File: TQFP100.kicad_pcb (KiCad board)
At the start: 2 copper layers, 0 parts

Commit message: Connected all traces
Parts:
- added IC1: 100-PQFP, Package_QFP:PQFP-100_14x20mm_P0.65mm, F.Cu at (152.0, 81.8)
- added J1: Conn_02x15_Counter_Clockwise, Connector_PinHeader_2.54mm:PinHeader_2x15_P2.54mm_Vertical, F.Cu at (134.5, 98.0)
- added J2: Conn_02x10_Odd_Even_MountingPin, Connector_PinHeader_2.54mm:PinHeader_2x10_P2.54mm_Vertical, F.Cu at (175.2, 92.9)
- added J3: Conn_02x15_Counter_Clockwise, Connector_PinHeader_2.54mm:PinHeader_2x15_P2.54mm_Vertical, F.Cu at (170.1, 65.0)
- added J4: Conn_02x10_Odd_Even_MountingPin, Connector_PinHeader_2.54mm:PinHeader_2x10_P2.54mm_Vertical, F.Cu at (129.4, 70.0)
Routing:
- net Net-(IC1-VSS_5): track 0.00 -> 16.2 mm
- net Net-(IC1-A05): track 0.00 -> 15.3 mm
- net Net-(IC1-~{INTAK}): track 0.00 -> 15.1 mm
- net Net-(IC1-D15): track 0.00 -> 14.9 mm
- net Net-(IC1-A22): track 0.00 -> 14.7 mm
- net Net-(IC1-~{LMCS}): track 0.00 -> 14.6 mm
- net Net-(IC1-~{BREQ}): track 0.00 -> 14.5 mm
- net Net-(IC1-A20): track 0.00 -> 14.2 mm
- net Net-(J1-Pin_29): track 0.00 -> 14.1 mm
- net Net-(IC1-A03): track 0.00 -> 14.1 mm
- net Net-(IC1-~{MCS1}): track 0.00 -> 14.1 mm
- net Net-(IC1-~{INT3}): track 0.00 -> 14.0 mm
- net Net-(IC1-A07): track 0.00 -> 13.8 mm
- net Net-(IC1-A24): track 0.00 -> 13.7 mm
- net Net-(IC1-D13): track 0.00 -> 13.7 mm
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
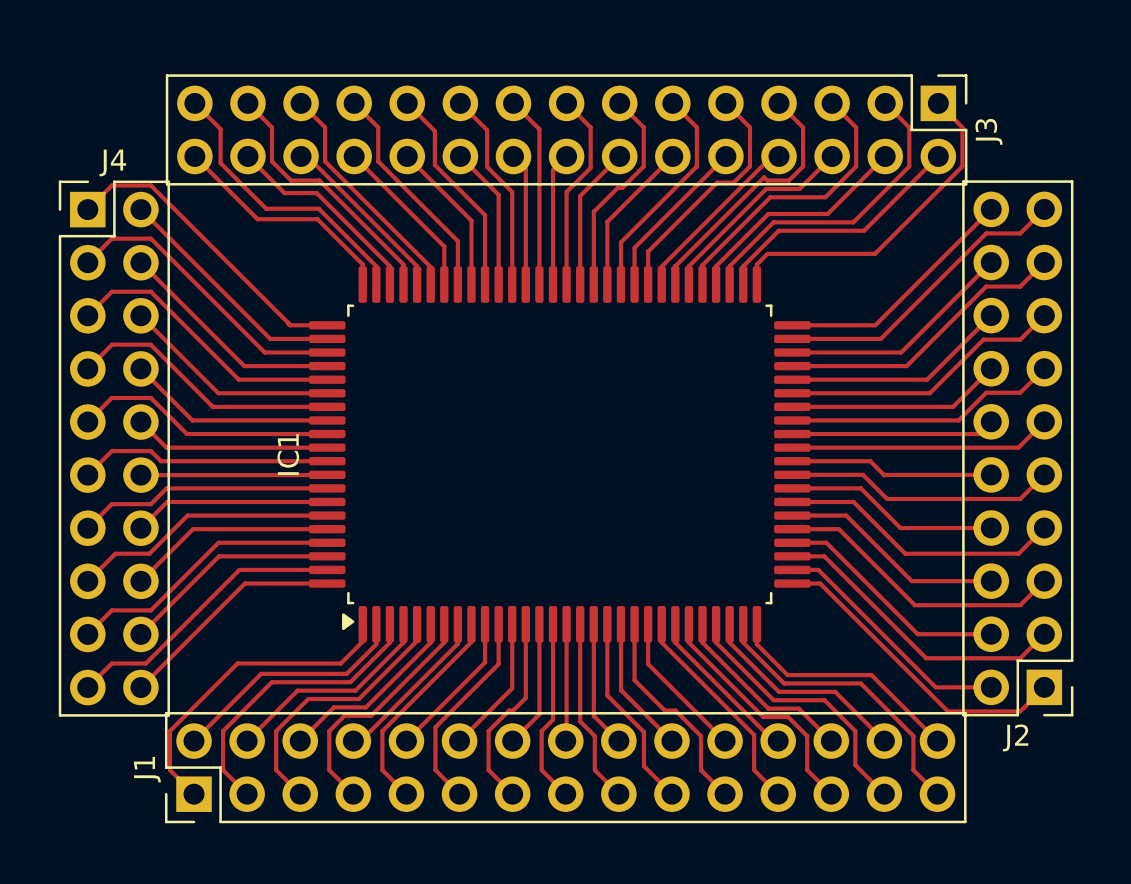
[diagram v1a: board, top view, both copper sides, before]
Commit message: Fixed the whole board, with correct names
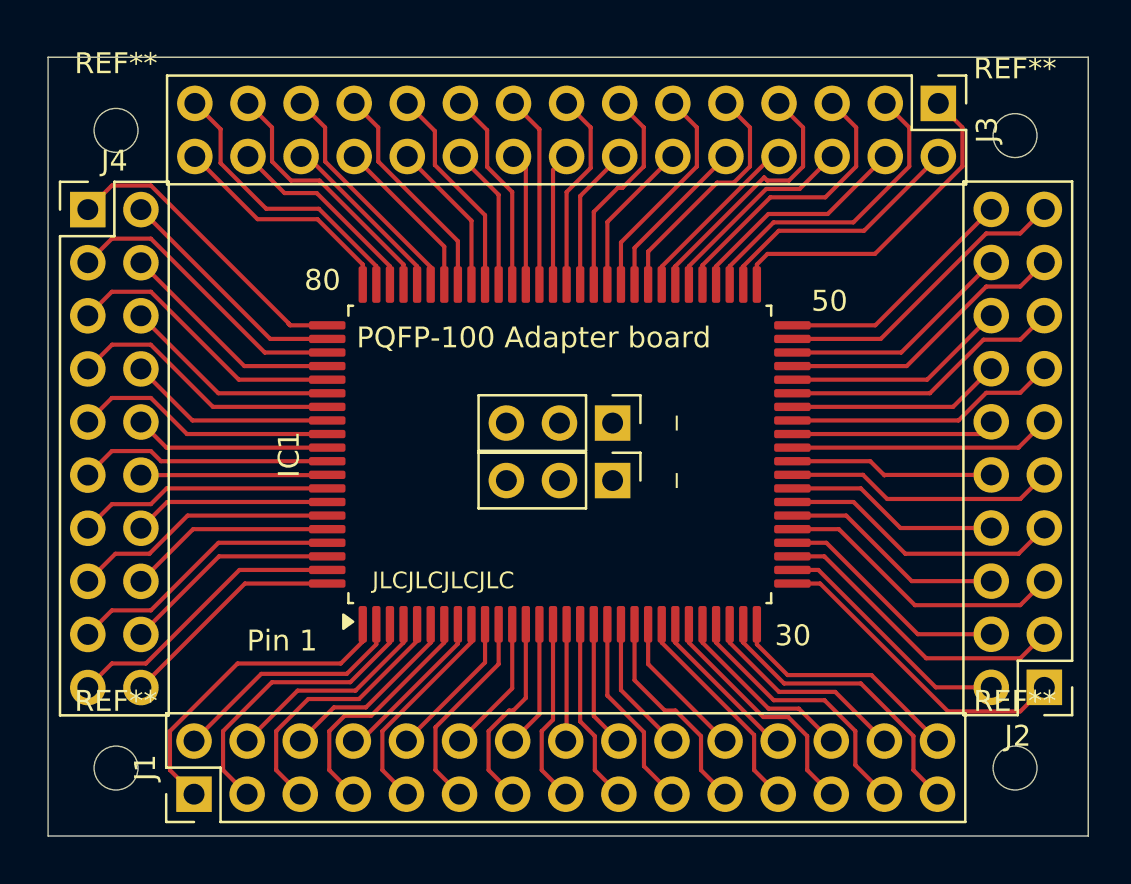
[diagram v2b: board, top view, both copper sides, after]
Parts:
- added REF**: MountingHole_2.1mm, MountingHole:MountingHole_2.1mm, F.Cu at (173.8, 96.8)
- added REF**: MountingHole_2.1mm, MountingHole:MountingHole_2.1mm, F.Cu at (130.8, 66.2)
- added REF**: MountingHole_2.1mm, MountingHole:MountingHole_2.1mm, F.Cu at (130.8, 96.8)
- added REF**: MountingHole_2.1mm, MountingHole:MountingHole_2.1mm, F.Cu at (173.8, 66.5)
- added _: PinHeader_1x03_P2.54mm_Vertical, Connector_PinHeader_2.54mm:PinHeader_1x03_P2.54mm_Vertical, F.Cu at (154.5, 83.0)
- added _: PinHeader_1x03_P2.54mm_Vertical, Connector_PinHeader_2.54mm:PinHeader_1x03_P2.54mm_Vertical, F.Cu at (154.5, 80.2)
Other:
- board outline added: 49.8 x 37.2 mm
- board text added: "30"
- board text added: "50"
- board text added: "80"
- board text added: "JLCJLCJLCJLC"
- board text added: "PQFP-100 Adapter board"
- board text added: "Pin 1"

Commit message: Larger pads to accommodate more ic, rev3
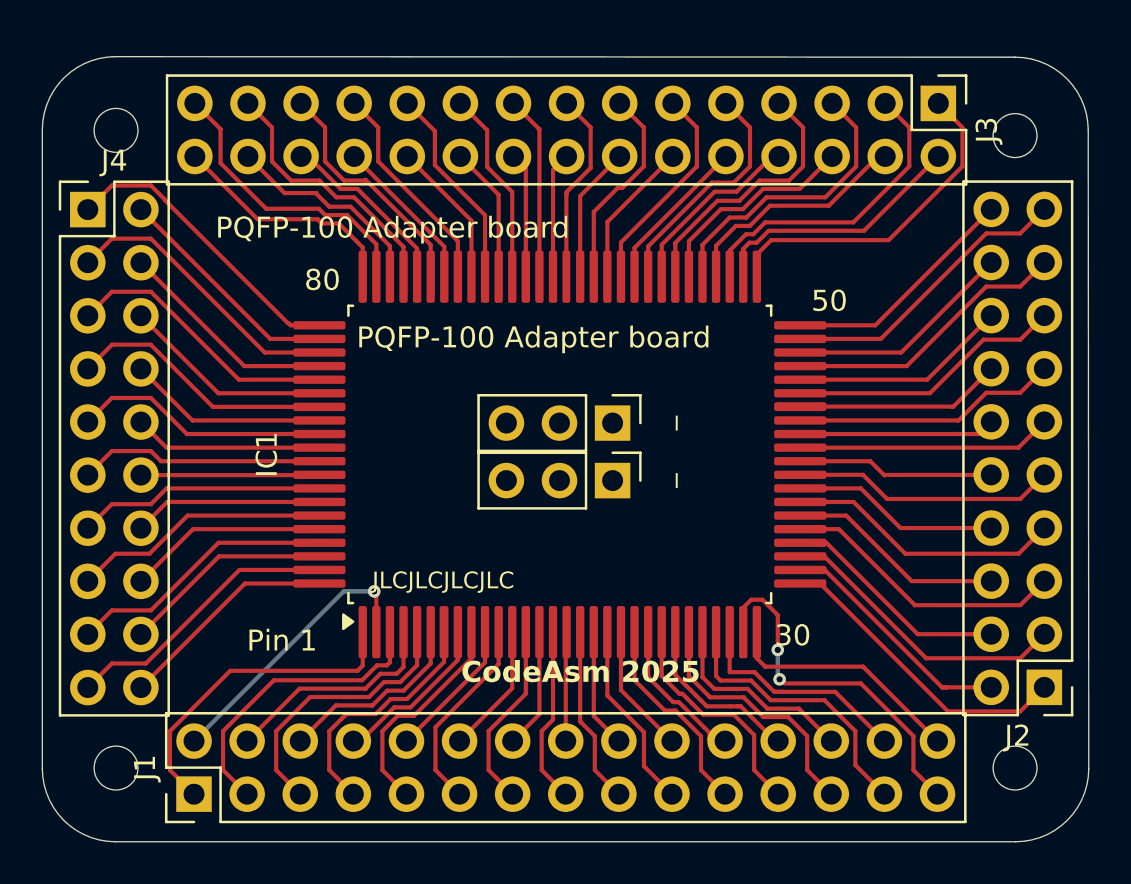
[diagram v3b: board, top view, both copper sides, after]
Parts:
- renumbered REF** to _
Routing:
- net Net-(IC1-A04): track 11.6 -> 14.5 mm, vias 0 -> 1
- net Net-(J1-Pin_29): track 14.1 -> 17.0 mm, vias 0 -> 2
- net Net-(IC1-~{BREQ}): track 14.5 -> 13.0 mm
- net Net-(IC1-D09): track 11.6 -> 10.2 mm
- net Net-(IC1-VSS_1): track 11.6 -> 13.0 mm
- net Net-(IC1-D12): track 9.90 -> 11.1 mm
- net Net-(IC1-A02): track 10.3 -> 11.5 mm
- net Net-(IC1-D13): track 13.7 -> 14.9 mm
- net Net-(IC1-A05): track 15.3 -> 16.4 mm
- net Net-(IC1-A25): track 9.84 -> 11.0 mm
- net Net-(IC1-A24): track 13.7 -> 14.9 mm
- net Net-(IC1-A28): track 11.2 -> 12.3 mm
- net Net-(IC1-A01): track 12.8 -> 13.9 mm
- net Net-(IC1-D10): track 8.65 -> 9.75 mm
- net Net-(IC1-A00): track 9.07 -> 10.2 mm
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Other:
- board size 49.8 x 37.2 mm -> 50.1 x 37.6 mm
- board text added: "1"
- board text added: "10"
- board text added: "100"
- board text added: "2"
- board text added: "20"
- board text added: "31"
- board text added: "40"
- board text added: "51"
- board text added: "60"
- board text added: "70"
- board text added: "81"
- board text added: "90"
- board text added: "CodeAsm 2025"
- board text added: "Optional ground"
